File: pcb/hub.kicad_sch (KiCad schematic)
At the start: 21 parts, among them U3 USB2514B, Y2 24MHz

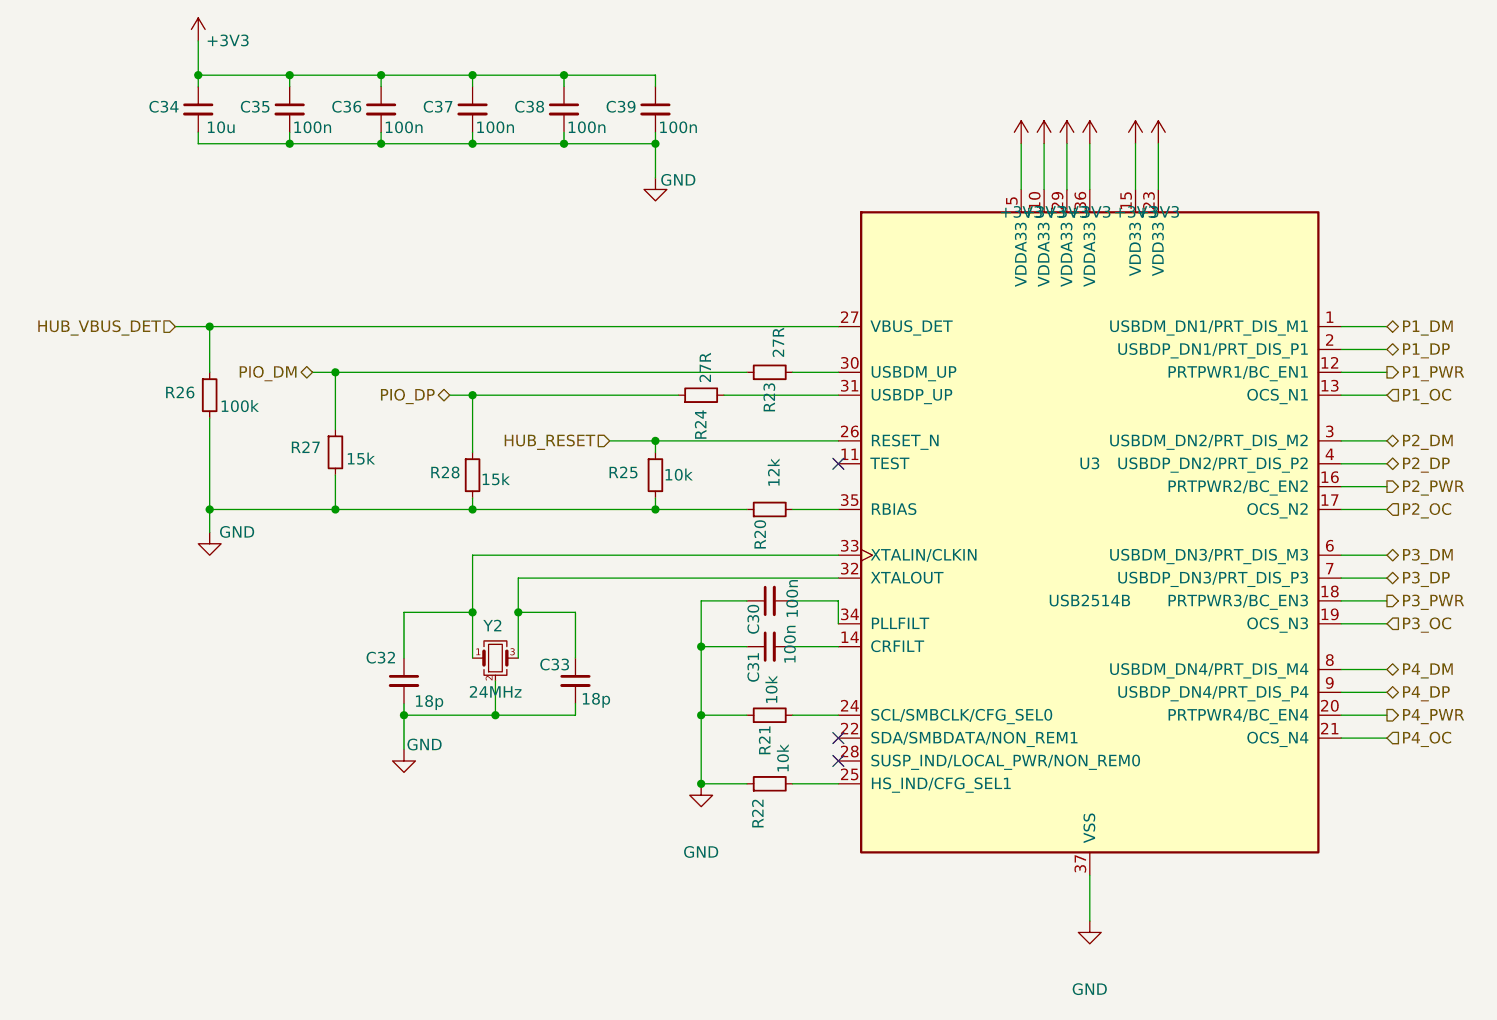
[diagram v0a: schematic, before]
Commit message: calculate the capacitor banks, and give every one of them a package
The question a value and a rating leave open is how much capacitance is actually there once the
voltage is across it, and the answer differs by package for the same value and rating. So the
requirement is derived bank by bank rather than taken from the vendors' part counts.

The charger's input is the binding case. Holding its input ripple to 100 mV with 5.4 A through the
inductor needs 8.6uF in circuit out of the 20uF fitted, so 43% has to survive 9V. The 5V rail needs
36% of what it carries and the system rail 27%. That last one is worth stating properly: ripple
alone would want only 2.5uF there, so the bank exists to answer load steps, and the realistic fast
step is the radio transmitting and the processor waking rather than the ports, which cannot step
quickly because the boost soft-starts over 4ms. At half an amp over five microseconds that is 25uF
against about 70uF effective.

43% is comfortable in 1206 and marginal in 0603 for a 10uF part at 9V, so the five capacitors on
the 9V nodes take 1206 and everything at 4.5V or under takes 0805. Decoupling goes to 0402, where
being near the pin matters more than the package, and the frequency- and loop-setting parts to
0603, where there is nothing to derate.

The answer to the open item is that the counts do not change: every bank is adequate as drawn
provided each part keeps roughly half of itself, which is what the package choice delivers. What is
left is a purchasing check rather than a design one.

Two asymmetries recorded. The 3.3V converter's vendor states that its recommended values anticipate
tolerance and bias derating and quotes 20% and 50%, so its table is nominal with the margin already
in it; the charger's and the boost's say nothing, so there the derating is ours to carry. And the
processor specifies an effective tolerance rather than a nominal one -- its core regulator's output
capacitor must be 4.7uF +/-20% in circuit.

The checker's 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
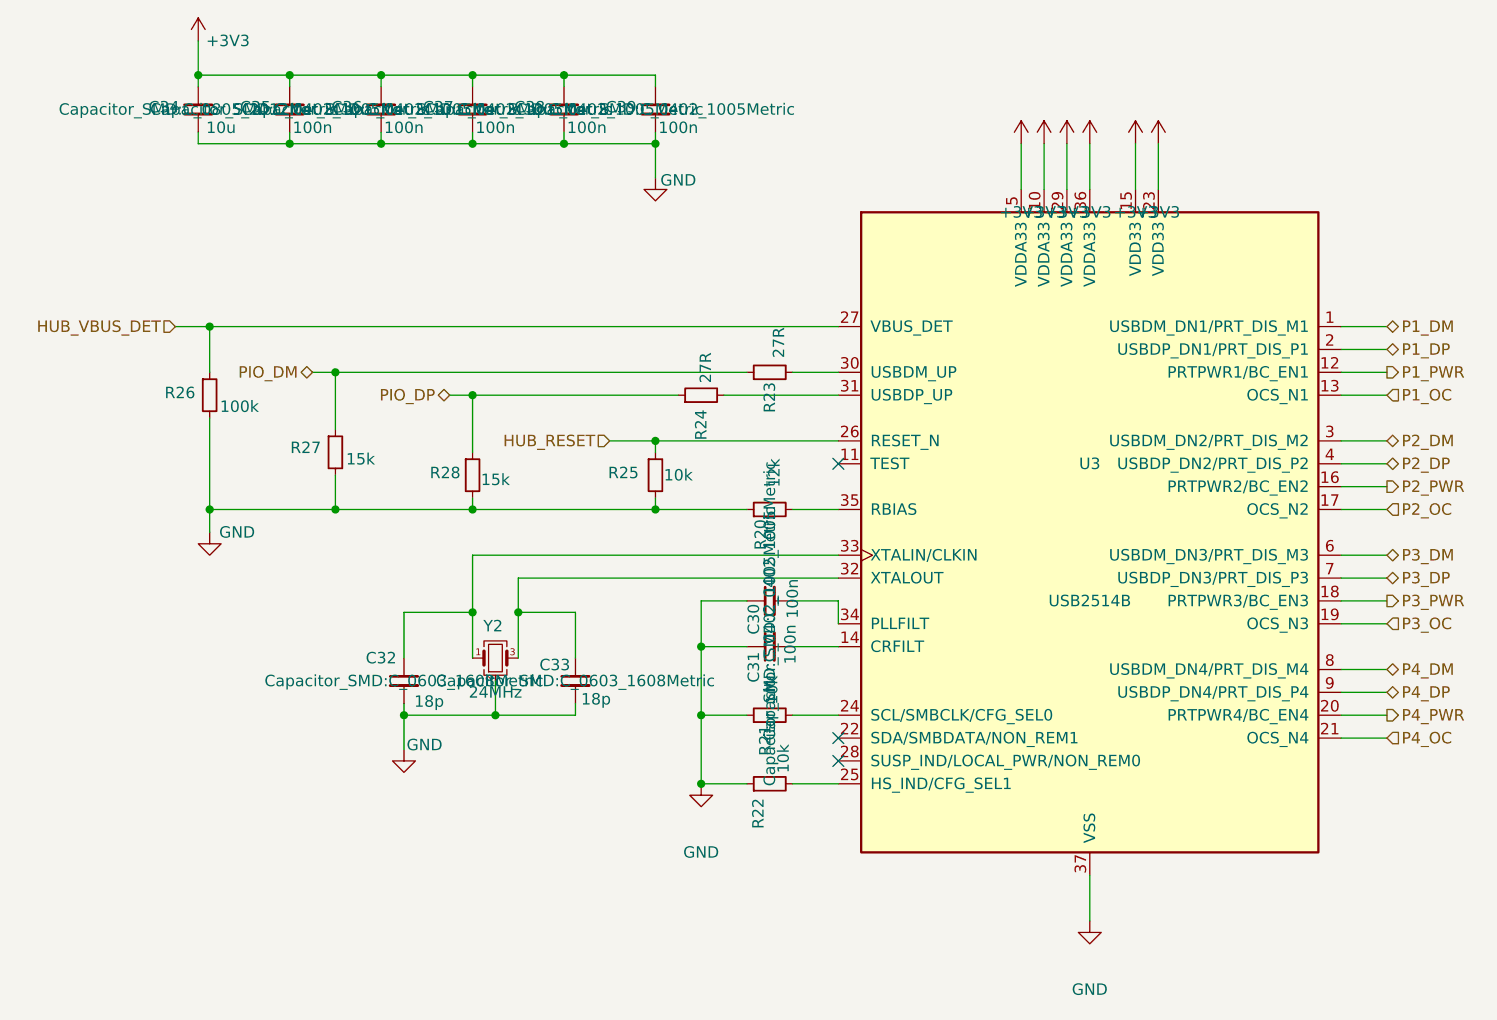
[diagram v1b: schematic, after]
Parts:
- C30, C31, C35, C36, C37, C38, C39: footprint (none) -> Capacitor_SMD:C_0402_1005Metric
- C32, C33: footprint (none) -> Capacitor_SMD:C_0603_1608Metric
- C34: footprint (none) -> Capacitor_SMD:C_0805_2012Metric
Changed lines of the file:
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@@
 			)
 		)
-		(property "Footprint" ""
+		(property "Footprint" "Capacitor_SMD:C_0603_1608Metric"
 			(at 146.05 143.51 0)
 			(show_name no)
@@
 			)
 		)
-		(property "Footprint" ""
+		(property "Footprint" "Capacitor_SMD:C_0402_1005Metric"
 			(at 167.64 139.7 0)
 			(show_name no)
@@
 			)
 		)
-		(property "Footprint" ""
+		(property "Footprint" "Capacitor_SMD:C_0402_1005Metric"
 			(at 114.3 80.01 0)
 			(show_name no)
@@
 			)
 		)
-		(property "Footprint" ""
+		(property "Footprint" "Capacitor_SMD:C_0402_1005Metric"
 			(at 167.64 134.62 0)
 			(show_name no)
@@
 			)
 		)
-		(property "Footprint" ""
+		(property "Footprint" "Capacitor_SMD:C_0805_2012Metric"
 			(at 104.14 80.01 0)
 			(show_name no)
@@
 			)
 		)
-		(property "Footprint" ""
+		(property "Footprint" "Capacitor_SMD:C_0603_1608Metric"
 			(at 127 143.51 0)
 			(show_name no)
@@
 			)
 		)
-		(property "Footprint" ""
+		(property "Footprint" "Capacitor_SMD:C_0402_1005Metric"
 			(at 144.78 80.01 0)
 			(show_name no)
@@
 			)
 		)
-		(property "Footprint" ""
+		(property "Footprint" "Capacitor_SMD:C_0402_1005Metric"
 			(at 124.46 80.01 0)
 			(show_name no)
@@
 			)
 		)
-		(property "Footprint" ""
+		(property "Footprint" "Capacitor_SMD:C_0402_1005Metric"
 			(at 134.62 80.01 0)
 			(show_name no)
@@
 			)
 		)
-		(property "Footprint" ""
+		(property "Footprint" "Capacitor_SMD:C_0402_1005Metric"
 			(at 154.94 80.01 0)
 			(show_name no)

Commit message: assign the footprints, and take the radio module's from its vendor
132 of the 135 parts now carry a footprint. Most follow from the package, the capacitors' follow
from the bias calculation, and the resistors are 0603 rather than 0402 because the board has room,
the first one runs bare on a bench, and a part you can get a probe or an iron onto is worth more
there than the millimetre it saves.

The radio module nearly went in hand-drawn. It has no footprint in any stock library, so the
obvious move was to draw one from the dimension drawing in its datasheet; the pitch, pad size and
pad length read off cleanly, but where each pad sits along its edge did not, and what I had was
inference from where things appeared in a rendered figure rather than a stated number. Raspberry Pi
publish a KiCad symbol and footprint, so that is what is fitted, in a project footprint library
beside the project symbol library. The figure agreed on everything it stated plainly, which says
nothing about the parts it did not.

Taking the official symbol also checked this project's hand-drawn one against theirs. All 21 pins
agree. Four carry different names -- their DI and DO, their nIRQ and WL_ON -- and nothing else
differs, so the pin numbering derived from the module's table is confirmed against its author
rather than merely self-consistent.

Four packages are fitted provisionally and are recorded as such, because what is unsettled about
them is invisible: the processor, the hub, the 3.3V converter and the power sink are in packages
whose library entries differ only in the size of the pad under the part. Body, pitch and pin count
are right; the pad is the nearest variant and wants checking against each vendor's land pattern,
since too small costs thermal performance and too large can wick the part off its pins.

Three parts are deliberately left without one. For the remaining inductors the footprint is the
part -- pad geometry differs between vendors at the same nominal size -- so choosing an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
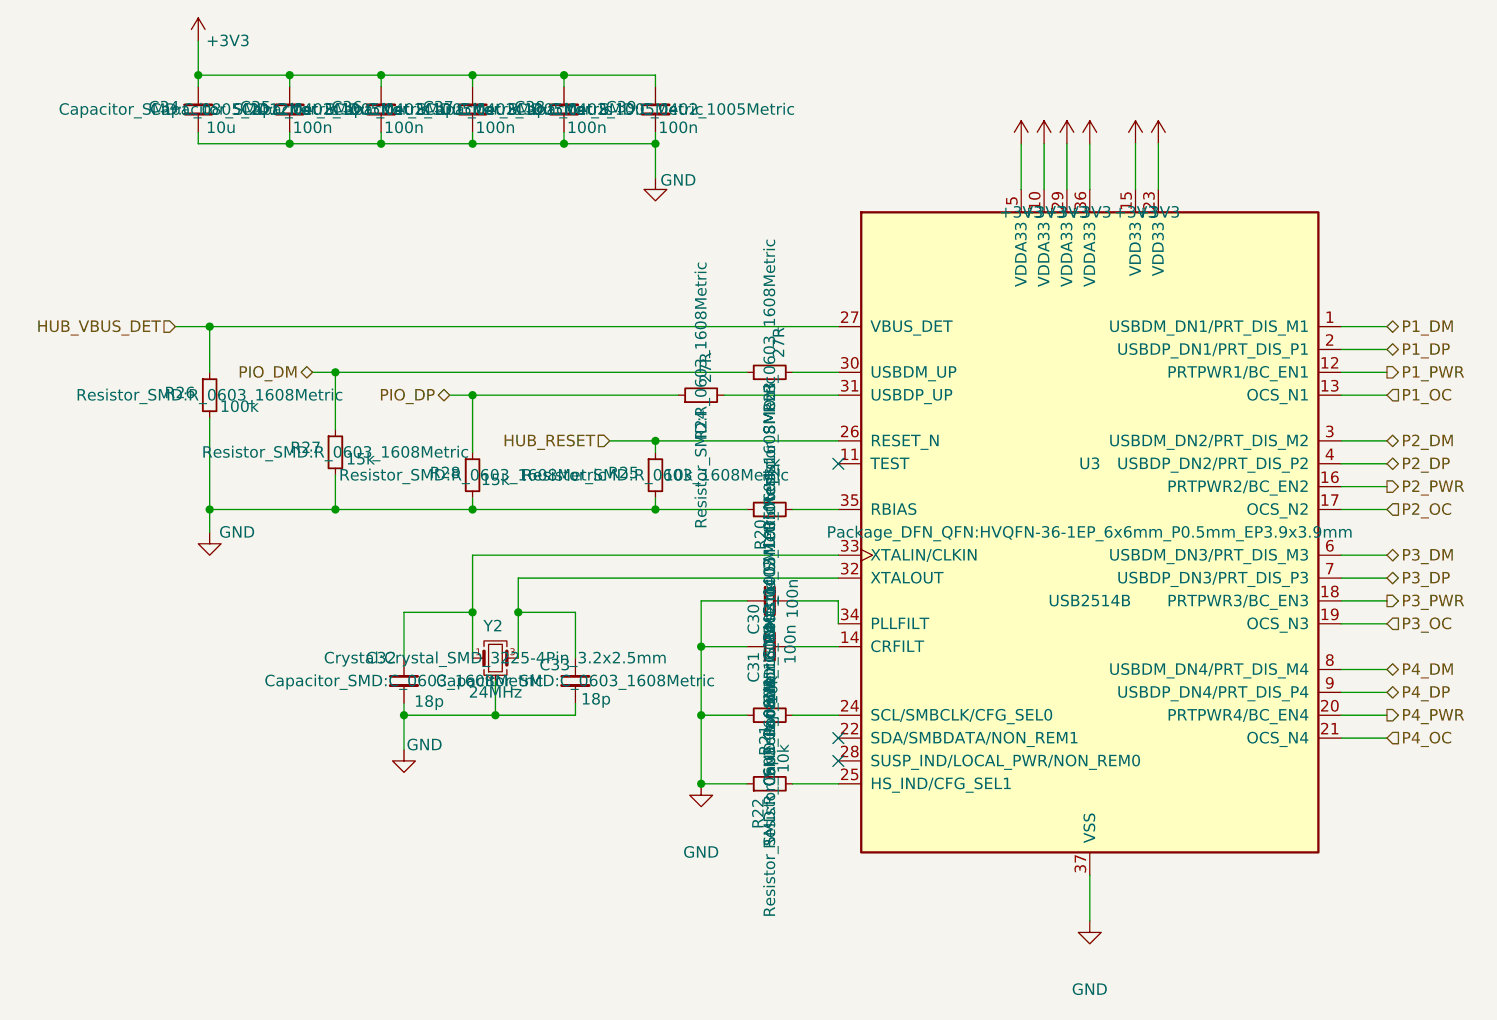
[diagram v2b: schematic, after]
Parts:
- R20, R21, R22, R23, R24, R25, R26, R27, R28: footprint (none) -> Resistor_SMD:R_0603_1608Metric
- U3: footprint (none) -> Package_DFN_QFN:HVQFN-36-1EP_6x6mm_P0.5mm_EP3.9x3.9mm
- Y2: footprint (none) -> Crystal:Crystal_SMD_3225-4Pin_3.2x2.5mm
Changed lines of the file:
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@@
 			)
 		)
-		(property "Footprint" ""
+		(property "Footprint" "Resistor_SMD:R_0603_1608Metric"
 			(at 167.64 147.32 0)
 			(show_name no)
@@
 			)
 		)
-		(property "Footprint" ""
+		(property "Footprint" "Resistor_SMD:R_0603_1608Metric"
 			(at 105.41 111.76 0)
 			(show_name no)
@@
 			)
 		)
-		(property "Footprint" ""
+		(property "Footprint" "Resistor_SMD:R_0603_1608Metric"
 			(at 167.64 109.22 0)
 			(show_name no)
@@
 			)
 		)
-		(property "Footprint" ""
+		(property "Footprint" "Resistor_SMD:R_0603_1608Metric"
 			(at 167.64 154.94 0)
 			(show_name no)
@@
 			)
 		)
-		(property "Footprint" ""
+		(property "Footprint" "Resistor_SMD:R_0603_1608Metric"
 			(at 119.38 118.11 0)
 			(show_name no)
@@
 			)
 		)
-		(property "Footprint" ""
+		(property "Footprint" "Crystal:Crystal_SMD_3225-4Pin_3.2x2.5mm"
 			(at 137.16 140.97 0)
 			(show_name no)
@@
 			)
 		)
-		(property "Footprint" ""
+		(property "Footprint" "Resistor_SMD:R_0603_1608Metric"
 			(at 160.02 111.76 0)
 			(show_name no)
@@
 			)
 		)
-		(property "Footprint" ""
+		(property "Footprint" "Resistor_SMD:R_0603_1608Metric"
 			(at 167.64 124.46 0)
 			(show_name no)
@@
 			)
 		)
-		(property "Footprint" ""
+		(property "Footprint" "Resistor_SMD:R_0603_1608Metric"
 			(at 154.94 120.65 0)
 			(show_name no)
@@
 			)
 		)
-		(property "Footprint" ""
+		(property "Footprint" "Package_DFN_QFN:HVQFN-36-1EP_6x6mm_P0.5mm_EP3.9x3.9mm"
 			(at 203.2 127 0)
 			(show_name no)
@@
 			)
 		)
-		(property "Footprint" ""
+		(property "Footprint" "Resistor_SMD:R_0603_1608Metric"
 			(at 134.62 120.65 0)
 			(show_name no)

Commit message: finish the footprints, and check the provisional ones against their vendors
Every one of the 135 parts now carries a footprint. The three that were fitted by matching body size
and pin count have been checked against their makers' own data, and two of the three were wrong.

The 3.3V converter's was wrong in kind rather than by a margin. Its maker's land pattern puts a
shaped thermal pad under the part -- a centre rectangle with fingers and tabs, thirteen pieces in
all -- and gives the signal pads extended toes beyond the body. The generic entry has a plain
rectangle and no toes. That shape is the thing in the drawing I could not interpret earlier and
assumed was a drafting flourish; it is the pattern. The library carries the real one under the
vendor's package code.

The hub's was wrong by 0.2mm each way. Its datasheet tabulates a recommended land pattern, not just
a package outline, and names a 3.70mm pad where the provisional entry had 3.90. Too large is the
direction that floats a part off its pins.

The power sink's was right: its vendor's exposed pad is 1.70 x 2.40 nominal against the fitted
1.65 x 2.38, a few hundredths under, which is the safe side. Worth confirming rather than assuming.

The two inductors took a footprint the library keeps under a family name, and its 4mm entries at
both heights carry identical pads -- which independently confirms the shared land pattern that made
the taller, higher-current part a free swap when it was chosen.

The hit rate is the lesson. Picking a footprint by body size and pin count got two of three wrong,
and neither error would have shown in the schematic, the netlist or any rules check -- only on a
board that did not assemble properly.

Co-Authored-By: Claude Opus 5 (1M context) <noreply@anthropic.com>
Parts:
- U3: footprint Package_DFN_QFN:HVQFN-36-1EP_6x6mm_P0.5mm_EP3.9x3.9mm -> Package_DFN_QFN:QFN-36-1EP_6x6mm_P0.5mm_EP3.7x3.7mm
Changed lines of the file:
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@@
 			)
 		)
-		(property "Footprint" "Package_DFN_QFN:HVQFN-36-1EP_6x6mm_P0.5mm_EP3.9x3.9mm"
+		(property "Footprint" "Package_DFN_QFN:QFN-36-1EP_6x6mm_P0.5mm_EP3.7x3.7mm"
 			(at 203.2 127 0)
 			(show_name no)
